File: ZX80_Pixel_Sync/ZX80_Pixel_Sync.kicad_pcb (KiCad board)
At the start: 2 copper layers, 45 x 18 mm, 7 parts, among them IC202 74LS74, J1 IC201, J2 To_Minstrel2

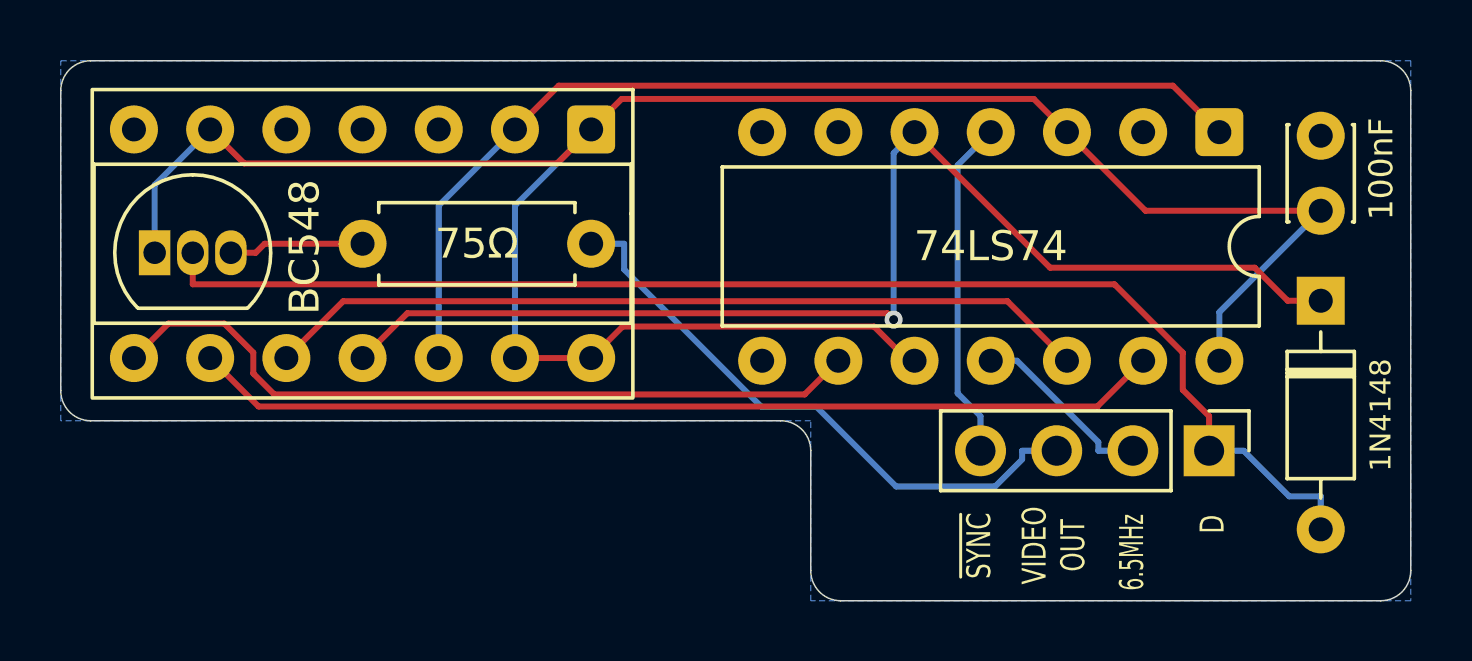
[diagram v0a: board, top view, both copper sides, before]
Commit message: Modified PCB layout after testing initial layout
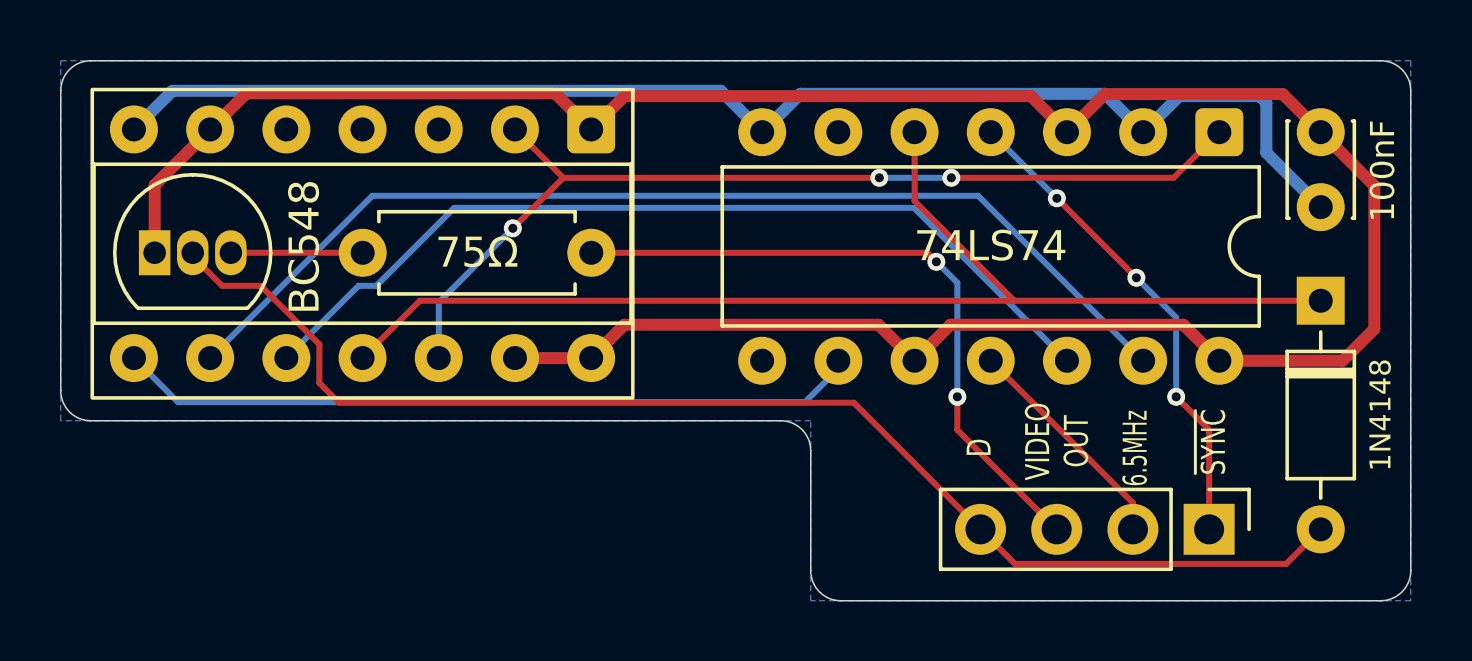
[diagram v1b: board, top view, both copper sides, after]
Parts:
- moved J2 2.62 mm to (86.9, 53.3)
- moved C1 2.38 mm to (90.6, 42.6), turned to 90 degrees
- moved R100 0.30 mm to (58.7, 44.1)
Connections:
- J2 pad 1: D -> ~{SYNC}
- J2 pad 4: ~{SYNC} -> D
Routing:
- net GND: track 0.00 -> 44.7 mm
- net +5V: track 74.1 -> 83.2 mm
- net ~{SYNC}: track 11.4 -> 16.3 mm, vias 0 -> 3
- net B: track 32.4 -> 35.6 mm
- net VIDEO: track 27.6 -> 30.2 mm
- net VIDEO_OUT: track 20.0 -> 22.2 mm, vias 0 -> 2
- net 6.5MHz: track 6.15 -> 7.58 mm
- net A: track 40.8 -> 39.7 mm, vias 1 -> 0
- net C: track 25.8 -> 24.8 mm
- net SYNC: track 33.4 -> 32.5 mm, vias 0 -> 3
- net D: track 44.1 -> 43.2 mm
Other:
- board text added: "ZX80 Pixel Glitch Fix for Minstrel 2 Rev. B"
- board text removed: "ZX80 Pixel Glitch Fix for Minstrel 2"
